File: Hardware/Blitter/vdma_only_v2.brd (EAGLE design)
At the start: 100 x 157.5 mm, 82 parts, among them IC1 74S08N, IC10 74HC191N, IC11 74HC191N, IC12 74HC191N, IC13 74HC191N, IC14 74HC191N, IC15 74HC191N, IC16 74HC573N, IC17 74HC573N, IC18 7432N, IC19 74LS257N, IC2 74HC191N, IC20 7430N, IC21 7400N, IC22 74LS257N, IC23 74LS257N, IC24 74LS257N, IC25 74LS257N, IC26 74LS257N, IC27 74LS257N, IC28 74LS257N, IC29 74LS257N, IC3 74HC573N, IC30 74HC573N, IC31 7400N, IC32 7432N, IC4 74HC191N, IC5 74HC573N, IC53 7404N, IC54 74LS07N, IC6 74HC573N, IC7 74HC573N, IC8 74HC573N, IC9 74LS74N, J1 TX25-40P-6ST-H1E, J2 TX25-40P-6ST-H1E

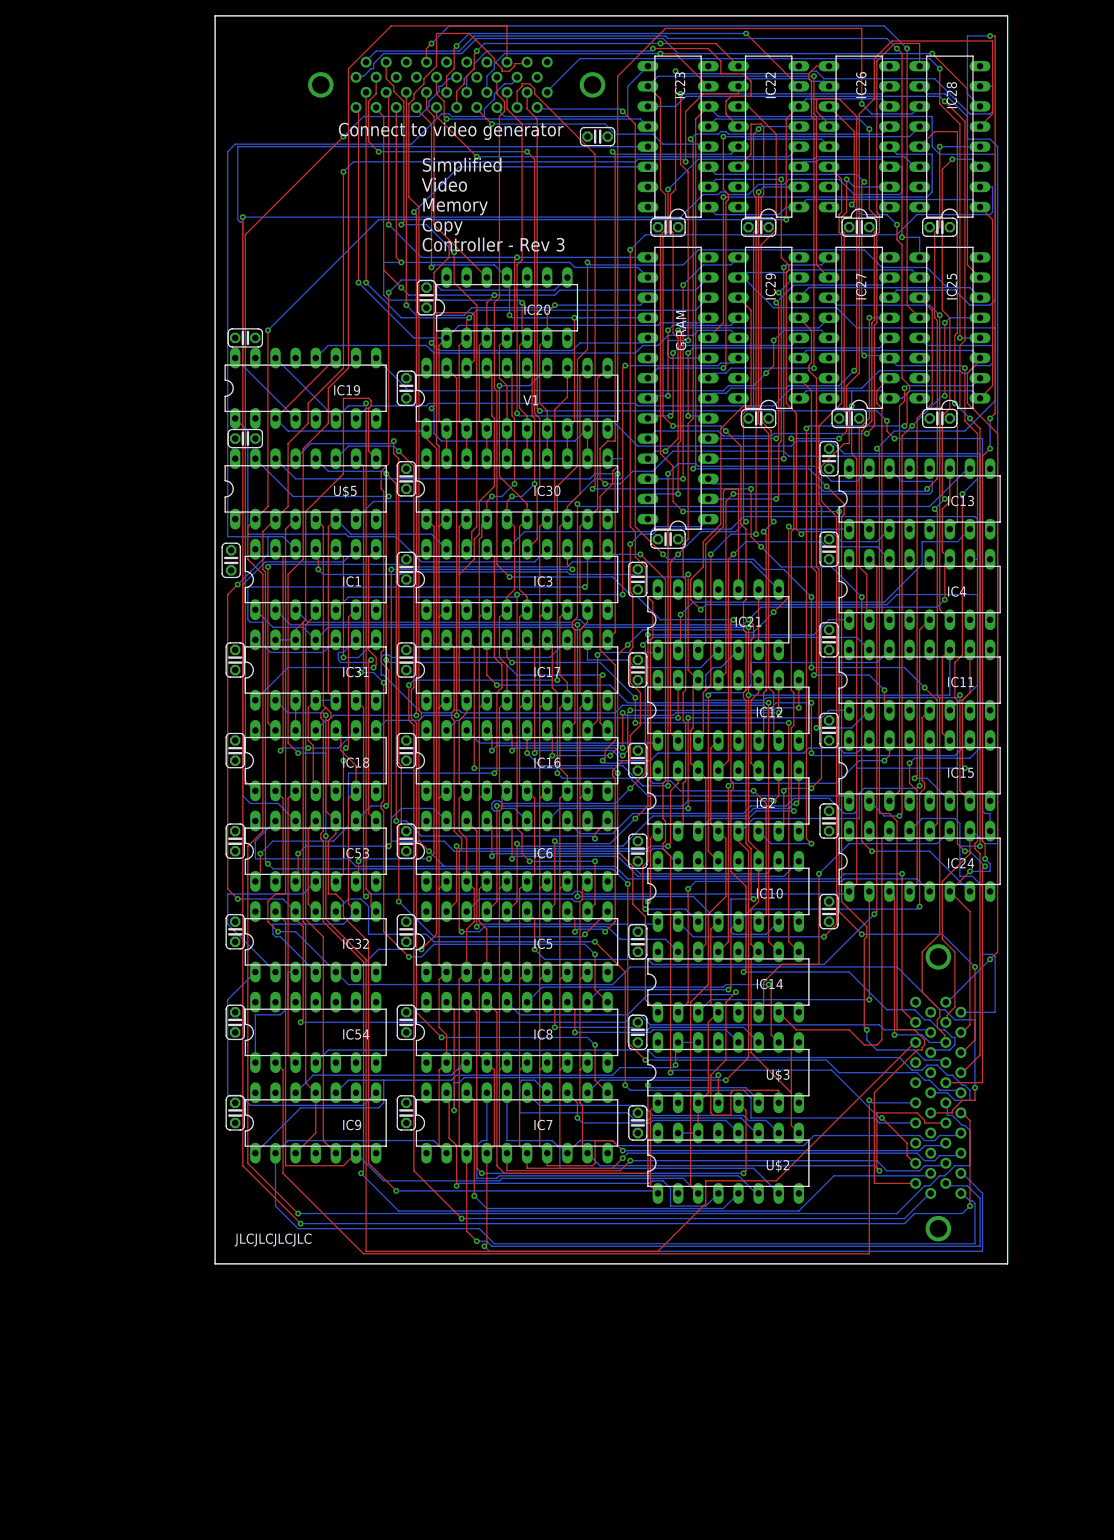
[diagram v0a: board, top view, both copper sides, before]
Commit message: update blitter
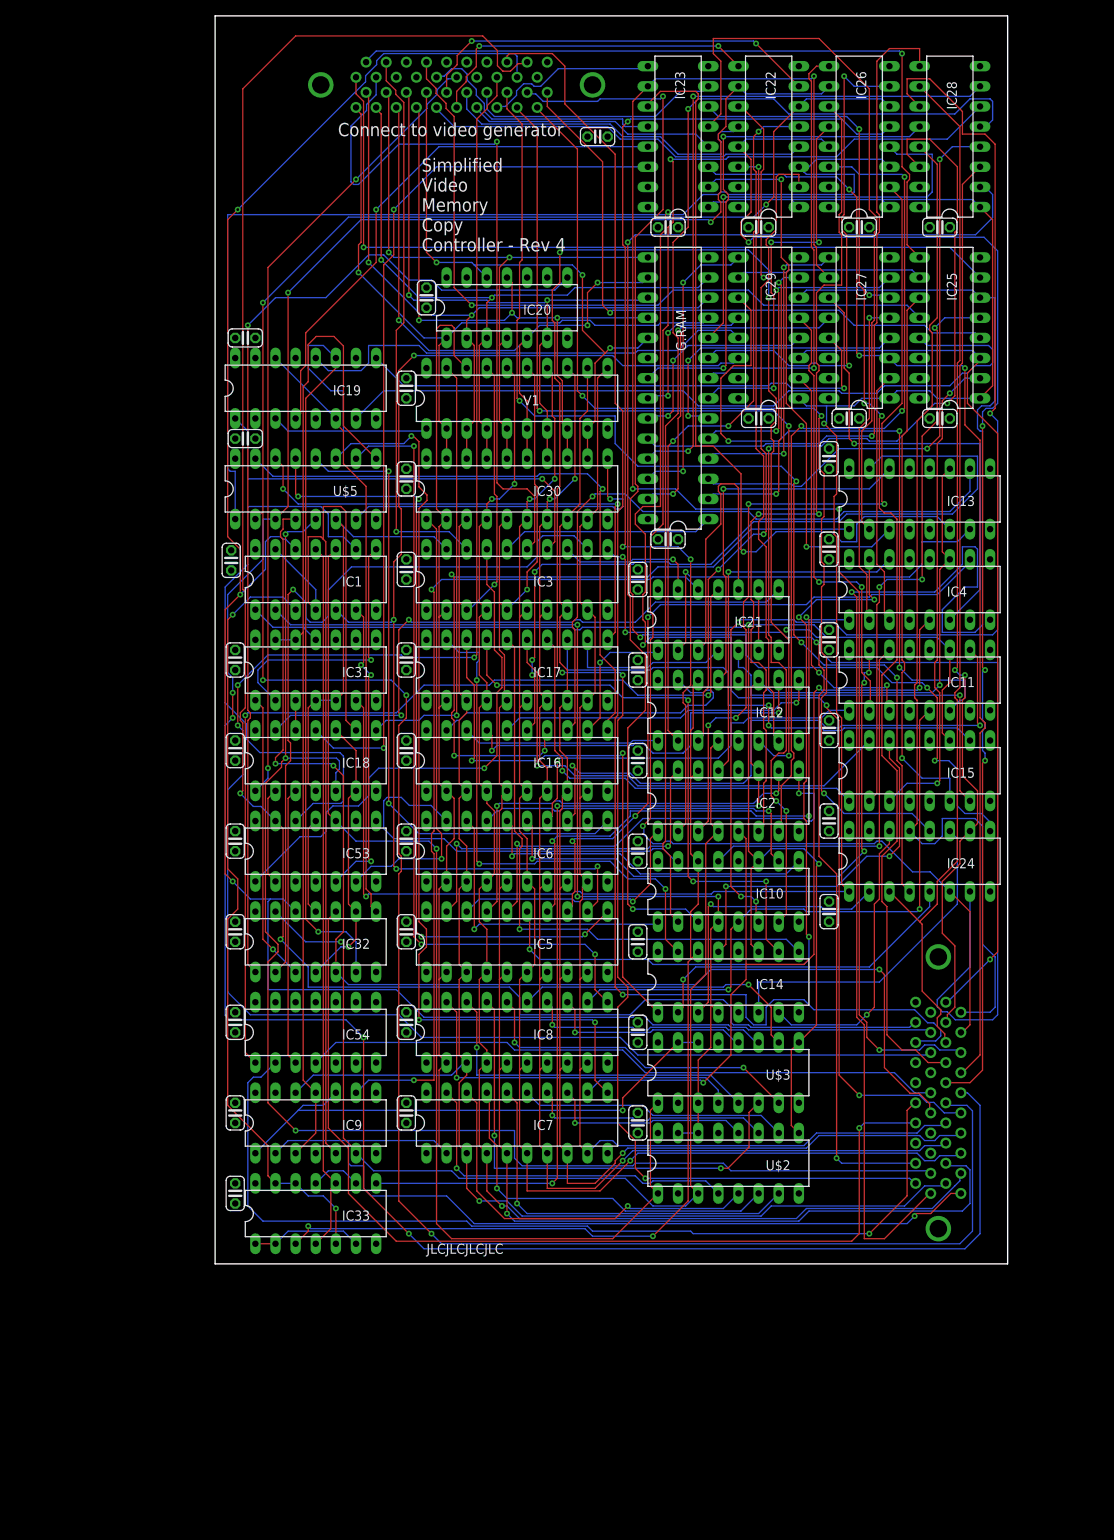
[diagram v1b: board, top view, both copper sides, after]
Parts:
- added C41: (no value), rcl:C025-024X044
- added IC33: 7400N, 74xx-us:DIL14
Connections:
- removed net !DMAIRQEN: IC32.2, IC53.4
- removed net N$100: IC32.1, IC9.8
- removed net N$213: IC20.8, IC53.9
- removed net N$214: IC31.9, IC53.8
- new net N$47: IC1.3, IC33.12, IC33.13, IC33.5
- new net N$48: IC33.11, IC33.9
- new net N$49: IC33.1, IC33.2, IC33.6
- new net N$58: IC21.12, IC9.9
- new net N$66: IC20.8, IC32.1
- new net XCLK: IC10.14, IC12.14, IC14.14, IC2.14, IC33.3
- net !DMACLK!/!IDLE!: now also IC1.10; no longer IC31.2
- net !DMAIRQ: now also IC21.11; no longer IC32.3
- net !XRELOAD: now also IC33.8; no longer IC1.3
- net DMACLK/!IDLE!: now also IC33.10, IC33.4; no longer IC10.14, IC12.14, IC14.14, IC2.14
- net DMAIRQEN: now also IC21.13; no longer IC53.3
- net GND: now also C41.2, IC31.10, IC31.9, IC33.7, IC53.3, IC53.9
- net N$16: now also IC31.1, IC32.3; no longer IC1.10, IC31.8
- net N$39: now also IC31.2; no longer IC31.1
- net TRANSEN: now also IC32.2; no longer IC31.10
- net VCC: now also C41.1, IC33.14
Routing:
- net N$66: track 0.00 -> 128.8 mm, vias 0 -> 1
- net XCLK: track 0.00 -> 122.9 mm, vias 0 -> 2
- net N$58: track 0.00 -> 107.8 mm, vias 0 -> 2
- net !DMAIRQ: track 16.0 -> 119.3 mm, vias 0 -> 2
- net N$47: track 0.00 -> 98.5 mm, vias 0 -> 2
- net N$213: track 94.9 -> 0.00 mm, vias 2 -> 0
- net CLK7: track 267.2 -> 181.7 mm, vias 2 -> 1
- net A12: track 276.1 -> 200.2 mm, vias 4 -> 1
- net A5: track 222.0 -> 152.7 mm, vias 3 -> 4
- net CLK3_5: track 175.5 -> 237.9 mm
- net DMAIRQEN: track 76.2 -> 18.2 mm, vias 4 -> 1
- net A2: track 274.0 -> 323.2 mm, vias 5 -> 6
- net N$37: track 111.5 -> 62.7 mm
- net VA8: track 149.1 -> 196.3 mm, vias 5 -> 3
- net A8: track 145.1 -> 190.6 mm, vias 5 -> 2
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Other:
- board text added: "Designed by Clyde Shaffer December 2020"
- board text added: "Simplified Video Memory Copy Controller - Rev 4"
- board text removed: "Designed by Clyde Shaffer November 2020"
- board text removed: "Simplified Video Memory Copy Controller - Rev 3"

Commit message: regrettably I don't remember what I changed since the last commit
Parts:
- removed IC10, IC11, IC12, IC13, IC14, IC15, IC2, IC4: 74HC191N, 74xx-us:DIL16
- removed IC16, IC17, IC3, IC30, IC5, IC6, IC7, IC8: 74HC573N, 74xx-us:DIL20
- removed IC19, IC22, IC23, IC24, IC25, IC26, IC27, IC28, IC29: 74LS257N, 74xx-us:DIL16
- removed IC33: 7400N, 74xx-us:DIL14
- removed U$2, U$3: CD40103, 000_mychips2:DIL16
- added BANKMUX, GMUX0, GMUX1, GMUX2, GMUX3, VMUX0, VMUX1, VMUX2, VMUX3: 74LS257N, 74xx-us:DIL16
- added CTR.H, CTR.W: CD40103, 000_mychips2:DIL16
- added GXFLIPPER, GYFLIPPER: 74AHC8541, 0_gametankparts:DIL20
- added GXH, GXL, GYH, GYL, VXH, VXL, VYH, VYL: 74HC163, 0_gametankparts:DIL16
- added PAD1, PAD2: (no value), wirepad:2,54/0,9
- added REG.COLOR, REG.FLAGS, REG.GX, REG.GY, REG.H, REG.VX, REG.VY, REG.W: 74HC573N, 74xx-us:DIL20
- moved C5 114.9 mm to (63.5, 2.54), turned to 0 degrees
- moved C27 80.3 mm to (52.1, 2.54), turned to 0 degrees
- moved C8 79.6 mm to (90.2, 109.2), turned to 0 degrees
- moved C31 76.0 mm to (78.7, 55.9)
- moved C32 76.0 mm to (68.6, 55.9)
- moved C33 76.0 mm to (55.9, 55.9)
- moved C34 76.0 mm to (44.5, 55.9)
- moved C29 75.5 mm to (55.9, 128.3), turned to 0 degrees
- moved C28 74.5 mm to (40.6, 2.54), turned to 0 degrees
- moved C25 74.3 mm to (52.1, 31.8), turned to 0 degrees
- moved C9 71.8 mm to (74.9, 2.54), turned to 0 degrees
- moved C26 69.1 mm to (40.6, 31.8), turned to 0 degrees
- moved C21 63.8 mm to (78.7, 109.2), turned to 0 degrees
- moved C24 63.7 mm to (78.7, 133.3), turned to 0 degrees
- moved C36 59.7 mm to (90.2, 133.3), turned to 0 degrees
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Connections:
- removed net N$107: IC12.13, IC13.14
- removed net N$109: IC14.13, IC15.14
- removed net XCLK: IC10.14, IC12.14, IC14.14, IC2.14, IC33.3
- new net GX-CARRY: GXH.10, GXL.15
- new net GY-CARRY: GYH.10, GYL.15
- new net N$68: GXFLIPPER.7, GXH.13
- new net N$72: GXFLIPPER.8, GXH.12
- new net N$73: GYFLIPPER.2, GYL.14
- new net N$74: GYFLIPPER.3, GYL.13
- new net N$75: GYFLIPPER.4, GYL.12
- new net N$76: GYFLIPPER.5, GYL.11
- new net N$77: GYFLIPPER.6, GYH.14
- new net N$78: GYFLIPPER.7, GYH.13
- new net N$79: GYFLIPPER.8, GYH.12
- new net N$80: GYFLIPPER.1, IC53.4
- new net N$81: GXFLIPPER.1, IC31.8
- new net ROWCOMPLETE: GYL.10, IC53.8, VYL.10
- new net VX-CARRY: VXH.10, VXL.15
- new net VY-CARRY: VYH.10, VYL.15
- net !COPYDONE: now also CTR.H.14, CTR.H.15; no longer U$3.14, U$3.15
- net !DMA-ENABLED: now also CTR.W.3; no longer IC12.4, IC2.4, U$2.3
- net !DMACLK!/!IDLE!: now also CTR.H.1, CTR.W.1; no longer U$2.1, U$3.1
- net !DMAMODE: now also GMUX0.1, GMUX1.1, GMUX2.1, GMUX3.1, VMUX0.1, VMUX1.1, VMUX2.1, VMUX3.1; no longer IC22.1, IC23.1, IC24.1, IC25.1, IC26.1, IC27.1, IC28.1, IC29.1
- net !DMASTART: now also CTR.H.9, CTR.W.9, GYH.9, GYL.9, VYH.9, VYL.9; no longer IC10.11, IC11.11, IC14.11, IC15.11, U$2.9, U$3.9
- net !ROWCOMPLETE: now also CTR.H.3, CTR.W.14, CTR.W.15, IC53.9; no longer IC10.4, IC14.4, U$2.14, U$2.15, U$3.3
- net !VOE: now also VMUX3.12; no longer IC25.12
- net !VWE: now also VMUX1.12; no longer IC23.12
- net !WRAP_X: now also REG.VX.12; no longer IC16.12
- net !WRAP_Y: now also REG.VY.12; no longer IC17.12
- net !XRELOAD: now also GXH.9, GXL.9, IC1.3, VXH.9, VXL.9; no longer IC12.11, IC13.11, IC2.11, IC33.8, IC4.11
- net A0: now also GMUX0.3, VMUX0.3; no longer IC22.3, IC26.3
- net A1: now also GMUX0.6, VMUX0.6; no longer IC22.6, IC26.6
- net A10: now also GMUX2.13, VMUX2.13; no longer IC24.13, IC28.13
- net A11: now also GMUX3.3, VMUX3.3; no longer IC25.3, IC29.3
- net A12: now also GMUX3.6, VMUX3.6; no longer IC25.6, IC29.6
- net A13: now also GMUX3.10, VMUX3.10; no longer IC25.10, IC29.10
- net A2: now also GMUX0.10, VMUX0.10; no longer IC22.10, IC26.10
- net A3: now also GMUX0.13, VMUX0.13; no longer IC22.13, IC26.13
- net A4: now also GMUX1.3, VMUX1.3; no longer IC23.3, IC27.3
- net A5: now also GMUX1.6, VMUX1.6; no longer IC23.6, IC27.6
- net A6: now also GMUX1.10, VMUX1.10; no longer IC23.10, IC27.10
- net A7: now also GMUX2.3, VMUX2.3; no longer IC24.3, IC28.3
- net A8: now also GMUX2.6, VMUX2.6; no longer IC24.6, IC28.6
- net A9: now also GMUX2.10, VMUX2.10; no longer IC24.10, IC28.10
- net COLORFILL: now also GMUX3.14, REG.GX.12; no longer IC29.14, IC5.12
- net D0: now also REG.COLOR.2, REG.FLAGS.2, REG.GX.2, REG.GY.2, REG.H.2, REG.VX.2, REG.VY.2, REG.W.2; no longer IC16.2, IC17.2, IC3.2, IC30.2, IC5.2, IC6.2, IC7.2, IC8.2
- net D1: now also REG.COLOR.3, REG.FLAGS.3, REG.GX.3, REG.GY.3, REG.H.3, REG.VX.3, REG.VY.3, REG.W.3; no longer IC16.3, IC17.3, IC3.3, IC30.3, IC5.3, IC6.3, IC7.3, IC8.3
- net D2: now also REG.COLOR.4, REG.FLAGS.4, REG.GX.4, REG.GY.4, REG.H.4, REG.VX.4, REG.VY.4, REG.W.4; no longer IC16.4, IC17.4, IC3.4, IC30.4, IC5.4, IC6.4, IC7.4, IC8.4
- net D3: now also REG.COLOR.5, REG.FLAGS.5, REG.GX.5, REG.GY.5, REG.H.5, REG.VX.5, REG.VY.5, REG.W.5; no longer IC16.5, IC17.5, IC3.5, IC30.5, IC5.5, IC6.5, IC7.5, IC8.5
- net D4: now also REG.COLOR.6, REG.FLAGS.6, REG.GX.6, REG.GY.6, REG.H.6, REG.VX.6, REG.VY.6, REG.W.6; no longer IC16.6, IC17.6, IC3.6, IC30.6, IC5.6, IC6.6, IC7.6, IC8.6
- net D5: now also REG.COLOR.7, REG.FLAGS.7, REG.GX.7, REG.GY.7, REG.H.7, REG.VX.7, REG.VY.7, REG.W.7; no longer IC16.7, IC17.7, IC3.7, IC30.7, IC5.7, IC6.7, IC7.7, IC8.7
- net D6: now also REG.COLOR.8, REG.FLAGS.8, REG.GX.8, REG.GY.8, REG.H.8, REG.VX.8, REG.VY.8, REG.W.8; no longer IC16.8, IC17.8, IC3.8, IC30.8, IC5.8, IC6.8, IC7.8, IC8.8
- net D7: now also REG.COLOR.9, REG.FLAGS.9, REG.GX.9, REG.GY.9, REG.H.9, REG.VX.9, REG.VY.9, REG.W.9; no longer IC16.9, IC17.9, IC3.9, IC30.9, IC5.9, IC6.9, IC7.9, IC8.9
- net DD0: now also REG.COLOR.19; no longer IC30.19
- net DD1: now also REG.COLOR.18; no longer IC30.18
- net DD2: now also REG.COLOR.17; no longer IC30.17
- net DD3: now also REG.COLOR.16; no longer IC30.16
- net DD4: now also REG.COLOR.15; no longer IC30.15
- net DD5: now also REG.COLOR.14; no longer IC30.14
- net DD6: now also REG.COLOR.13; no longer IC30.13
- net DD7: now also REG.COLOR.12; no longer IC30.12
- net DMA-ENABLED: now also GXH.7, GXL.7, GYH.7, GYL.7, VXH.7, VXL.7, VYH.7, VYL.7; no longer IC1.13
- net DMACLK/!IDLE!: now also GXH.2, GXL.2, GYH.2, GYL.2, VXH.2, VXL.2, VYH.2, VYL.2; no longer IC33.10, IC33.4
- net DMAIRQEN: now also REG.FLAGS.13; no longer IC3.13
- net DMAMODE: now also REG.FLAGS.19; no longer IC3.19
- net GND: now also BANKMUX.15, BANKMUX.8, CTR.H.13, CTR.H.8, CTR.W.13, CTR.W.8, GMUX0.15, GMUX0.8, GMUX1.15, GMUX1.8, GMUX2.15, GMUX2.8, GMUX3.15, GMUX3.8, GXFLIPPER.10, GXFLIPPER.11, GXH.8, GXL.8, GYFLIPPER.10, GYFLIPPER.11, GYH.8, GYL.8, PAD1.1, PAD2.1, REG.COLOR.10, REG.FLAGS.1, REG.FLAGS.10, REG.GX.1, REG.GX.10, REG.GY.1, REG.GY.10, REG.H.1, REG.H.10, REG.VX.1, REG.VX.10, REG.VY.1, REG.VY.10, REG.W.1, REG.W.10, VMUX0.15, VMUX0.8, VMUX1.15, VMUX1.8, VMUX2.15, VMUX2.8, VMUX3.15, VMUX3.8, VXH.8, VXL.8, VYH.8, VYL.8; no longer IC10.8, IC11.4, IC11.8, IC11.9, IC12.5, IC12.8, IC13.4, IC13.5, IC13.8, IC13.9, IC14.5, IC14.8, IC15.4, IC15.5, IC15.8, IC15.9, IC16.1, IC16.10, IC17.1, IC17.10, IC19.15, IC19.8, IC2.8, IC22.15, IC22.8, IC23.15, IC23.8, IC24.15, IC24.8, IC25.15, IC25.8, IC26.15, IC26.8, IC27.15, IC27.8, IC28.15, IC28.8, IC29.15, IC29.8, IC3.1, IC3.10, IC30.10, IC31.10, IC31.9, IC33.7, IC4.4, IC4.8, IC4.9, IC5.1, IC5.10, IC53.3, IC53.9, IC6.1, IC6.10, IC7.1, IC7.10, IC8.1, IC8.10, U$2.13, U$2.8, U$3.13, U$3.8
- net GRAMBANK: now also REG.FLAGS.16; no longer IC3.16
- net N$1: now also GMUX0.4; no longer IC26.4
- net N$10: now also GMUX2.9; no longer IC28.9
- net N$108: now also REG.W.11; no longer IC7.11
- net N$11: now also GMUX2.12; no longer IC28.12
- net N$111: now also REG.H.11; no longer IC8.11
- net N$113: now also REG.VY.19, VYL.3; no longer IC14.15, IC17.19
- net N$114: now also REG.VY.18, VYL.4; no longer IC14.1, IC17.18
- net N$115: now also REG.VY.17, VYL.5; no longer IC14.10, IC17.17
- net N$116: now also REG.VY.16, VYL.6; no longer IC14.9, IC17.16
- net N$117: now also REG.VX.15, VXH.3; no longer IC13.15, IC16.15
- net N$118: now also REG.VX.14, VXH.4; no longer IC13.1, IC16.14
- net N$119: now also REG.VX.13, VXH.5; no longer IC13.10, IC16.13
- net N$12: now also GMUX3.4; no longer IC29.4
- net N$121: now also REG.VX.19, VXL.3; no longer IC12.15, IC16.19
- net N$122: now also REG.VX.18, VXL.4; no longer IC12.1, IC16.18
- net N$123: now also REG.VX.17, VXL.5; no longer IC12.10, IC16.17
- net N$124: now also REG.VX.16, VXL.6; no longer IC12.9, IC16.16
- net N$125: now also REG.COLOR.11; no longer IC30.11
- net N$13: now also GMUX3.7; no longer IC29.7
- net N$14: now also GMUX3.9; no longer IC29.9
- net N$15: now also VMUX1.14; no longer IC23.14
- net N$160: now also VMUX0.5, VXL.13; no longer IC12.2, IC22.5
- net N$161: now also VMUX0.11, VXL.12; no longer IC12.6, IC22.11
- net N$162: now also VMUX0.14, VXL.11; no longer IC12.7, IC22.14
- net N$163: now also VMUX1.2, VXH.14; no longer IC13.3, IC23.2
- net N$164: now also VMUX1.5, VXH.13; no longer IC13.2, IC23.5
- net N$165: now also VMUX1.11, VXH.12; no longer IC13.6, IC23.11
- net N$167: now also VMUX2.5, VYL.13; no longer IC14.2, IC24.5
- net N$168: now also VMUX2.11, VYL.12; no longer IC14.6, IC24.11
- net N$169: now also VMUX2.14, VYL.11; no longer IC14.7, IC24.14
- net N$17: now also GMUX1.12; no longer IC27.12
- net N$170: now also VMUX3.2, VYH.14; no longer IC15.3, IC25.2
- net N$171: now also VMUX3.5, VYH.13; no longer IC15.2, IC25.5
- net N$172: now also VMUX3.11, VYH.12; no longer IC15.6, IC25.11
- net N$173: now also GMUX0.2, GXFLIPPER.19; no longer IC2.3, IC26.2
- net N$174: now also GMUX0.5, GXFLIPPER.18; no longer IC2.2, IC26.5
- net N$175: now also GMUX0.11, GXFLIPPER.17; no longer IC2.6, IC26.11
- net N$176: now also GMUX0.14, GXFLIPPER.16; no longer IC2.7, IC26.14
- net N$177: now also GMUX1.2, GXFLIPPER.15; no longer IC27.2, IC4.3
- net N$178: now also GMUX1.5, GXFLIPPER.14; no longer IC27.5, IC4.2
- net N$179: now also GMUX1.11, GXFLIPPER.13; no longer IC27.11, IC4.6
- net N$18: now also GMUX3.12; no longer IC29.12
- net N$180: now also GMUX2.2, GYFLIPPER.19; no longer IC10.3, IC28.2
- net N$181: now also GMUX2.5, GYFLIPPER.18; no longer IC10.2, IC28.5
- net N$182: now also GMUX2.11, GYFLIPPER.17; no longer IC10.6, IC28.11
- net N$183: now also GMUX2.14, GYFLIPPER.16; no longer IC10.7, IC28.14
- net N$184: now also GMUX3.2, GYFLIPPER.15; no longer IC11.3, IC29.2
- net N$185: now also GMUX3.5, GYFLIPPER.14; no longer IC11.2, IC29.5
- net N$186: now also GMUX3.11, GYFLIPPER.13; no longer IC11.6, IC29.11
- net N$19: now also GYL.3, REG.GY.19; no longer IC10.15, IC6.19
- net N$2: now also GMUX0.7; no longer IC26.7
- net N$20: now also GYL.4, REG.GY.18; no longer IC10.1, IC6.18
- net N$21: now also GYL.5, REG.GY.17; no longer IC10.10, IC6.17
- net N$22: now also GYL.6, REG.GY.16; no longer IC10.9, IC6.16
- net N$23: now also GXH.3, REG.GX.15; no longer IC4.15, IC5.15
- net N$24: now also GXH.4, REG.GX.14; no longer IC4.1, IC5.14
- net N$25: now also GXH.5, REG.GX.13; no longer IC4.10, IC5.13
- net N$26: now also GYH.3, REG.GY.15; no longer IC11.15, IC6.15
- net N$27: now also GXL.3, REG.GX.19; no longer IC2.15, IC5.19
- net N$28: now also GXL.4, REG.GX.18; no longer IC2.1, IC5.18
- net N$29: now also GXL.5, REG.GX.17; no longer IC2.10, IC5.17
- net N$3: now also GMUX0.9; no longer IC26.9
- net N$30: now also GXL.6, REG.GX.16; no longer IC2.9, IC5.16
- net N$31: now also GYH.4, REG.GY.14; no longer IC11.1, IC6.14
- net N$32: now also GYH.5, REG.GY.13; no longer IC11.10, IC6.13
- net N$35: now also REG.VY.15, VYH.3; no longer IC15.15, IC17.15
- net N$36: now also REG.VY.14, VYH.4; no longer IC15.1, IC17.14
- net N$37: now also REG.VY.13, VYH.5; no longer IC15.10, IC17.13
- net N$4: now also GMUX0.12; no longer IC26.12
- net N$41: now also REG.COLOR.1; no longer IC30.1
- net N$42: now also GXFLIPPER.5, GXL.11; no longer IC2.13, IC4.14
- net N$43: now also GXFLIPPER.4, GXL.12; no longer IC10.13, IC11.14
- net N$47: now also GXFLIPPER.3, GXL.13; no longer IC1.3, IC33.12, IC33.13, IC33.5
- net N$48: now also GXFLIPPER.2, GXL.14; no longer IC33.11, IC33.9
- net N$49: now also GXFLIPPER.6, GXH.14; no longer IC33.1, IC33.2, IC33.6
- net N$5: now also GMUX1.4; no longer IC27.4
- net N$50: now also BANKMUX.4, VMUX1.13; no longer IC19.4, IC23.13
- net N$51: now also CTR.H.4, REG.H.19; no longer IC8.19, U$3.4
- net N$52: now also CTR.H.5, REG.H.18; no longer IC8.18, U$3.5
- net N$53: now also CTR.H.6, REG.H.17; no longer IC8.17, U$3.6
- net N$54: now also CTR.H.7, REG.H.16; no longer IC8.16, U$3.7
- net N$55: now also CTR.H.10, REG.H.15; no longer IC8.15, U$3.10
- net N$56: now also CTR.H.11, REG.H.14; no longer IC8.14, U$3.11
- net N$57: now also CTR.H.12, REG.H.13; no longer IC8.13, U$3.12
- net N$59: now also CTR.W.4, REG.W.19; no longer IC7.19, U$2.4
- net N$6: now also GMUX1.7; no longer IC27.7
- net N$60: now also CTR.W.5, REG.W.18; no longer IC7.18, U$2.5
- net N$61: now also CTR.W.6, REG.W.17; no longer IC7.17, U$2.6
- net N$62: now also CTR.W.7, REG.W.16; no longer IC7.16, U$2.7
- net N$63: now also CTR.W.10, REG.W.15; no longer IC7.15, U$2.10
- net N$64: now also CTR.W.11, REG.W.14; no longer IC7.14, U$2.11
- net N$65: now also CTR.W.12, REG.W.13; no longer IC7.13, U$2.12
- net N$67: now also BANKMUX.7, VMUX3.13; no longer IC19.7, IC25.13
- net N$69: now also BANKMUX.9, GMUX1.13; no longer IC19.9, IC27.13
- net N$7: now also GMUX1.9; no longer IC27.9
- net N$70: now also BANKMUX.12, GMUX3.13; no longer IC19.12, IC29.13
- net N$71: now also REG.VX.11; no longer IC16.11
- net N$8: now also GMUX2.4; no longer IC28.4
- net N$9: now also GMUX2.7; no longer IC28.7
- net N$94: now also REG.VY.11; no longer IC17.11
- net N$96: now also REG.GX.11; no longer IC5.11
- net N$98: now also REG.GY.11; no longer IC6.11
- net OFFSCR_X: now also VXH.11; no longer IC13.7
- net OFFSCR_Y: now also VYH.11; no longer IC15.7
- net TRANSEN: now also REG.FLAGS.12; no longer IC3.12
- net V/_G: now also BANKMUX.1, REG.FLAGS.14; no longer IC19.1, IC3.14
- net VA0: now also VMUX0.4; no longer IC22.4
- net VA1: now also VMUX0.7; no longer IC22.7
- net VA10: now also VMUX2.12; no longer IC24.12
- net VA11: now also VMUX3.4; no longer IC25.4
- net VA12: now also VMUX3.7; no longer IC25.7
- net VA13: now also VMUX3.9; no longer IC25.9
- net VA2: now also VMUX0.9; no longer IC22.9
- net VA3: now also VMUX0.12; no longer IC22.12
- net VA4: now also VMUX1.4; no longer IC23.4
- net VA5: now also VMUX1.7; no longer IC23.7
- net VA6: now also VMUX1.9; no longer IC23.9
- net VA7: now also VMUX2.4; no longer IC24.4
- net VA8: now also VMUX2.7; no longer IC24.7
- net VA9: now also VMUX2.9; no longer IC24.9
- net VCC: now also BANKMUX.10, BANKMUX.13, BANKMUX.16, BANKMUX.2, BANKMUX.5, CTR.H.16, CTR.H.2, CTR.W.16, CTR.W.2, GMUX0.16, GMUX1.14, GMUX1.16, GMUX2.16, GMUX3.16, GXFLIPPER.20, GXH.1, GXH.16, GXL.1, GXL.10, GXL.16, GYFLIPPER.20, GYH.1, GYH.16, GYL.1, GYL.16, IC1.13, REG.COLOR.20, REG.FLAGS.20, REG.GX.20, REG.GY.20, REG.H.20, REG.VX.20, REG.VY.20, REG.W.20, VMUX0.16, VMUX1.16, VMUX2.16, VMUX3.14, VMUX3.16, VXH.1, VXH.16, VXL.1, VXL.10, VXL.16, VYH.1, VYH.16, VYL.1, VYL.16; no longer IC10.16, IC11.16, IC12.16, IC13.16, IC14.16, IC15.16, IC16.20, IC17.20, IC19.10, IC19.13, IC19.16, IC19.2, IC19.5, IC2.16, IC22.16, IC23.16, IC24.16, IC25.14, IC25.16, IC26.16, IC27.14, IC27.16, IC28.16, IC29.16, IC3.20, IC30.20, IC33.14, IC4.16, IC5.20, IC6.20, IC7.20, IC8.20, U$2.16, U$2.2, U$3.16, U$3.2
- net VG_OE: now also BANKMUX.14, BANKMUX.6; no longer IC19.14, IC19.6
- net VG_WE: now also BANKMUX.11, BANKMUX.3; no longer IC19.11, IC19.3
- net VIDFLAGS: now also REG.FLAGS.11; no longer IC3.11
- net VIDPAGE: now also REG.FLAGS.18; no longer IC3.18
- net VNMI_ENABLE: now also REG.FLAGS.17; no longer IC3.17
- net VRAMBANK: now also REG.FLAGS.15; no longer IC3.15
- net XDIR: now also IC31.10, IC31.9, REG.W.12; no longer IC2.5, IC4.5, IC7.12
- net XODD: now also VMUX0.2, VXL.14; no longer IC12.3, IC22.2
- net YDIR: now also IC53.3, REG.H.12; no longer IC10.5, IC11.5, IC8.12
- net YODD: now also VMUX2.2, VYL.14; no longer IC14.3, IC24.2
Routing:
- net A2: track 323.2 -> 0.00 mm, vias 6 -> 0
- net A0: track 295.7 -> 0.00 mm, vias 4 -> 0
- net CLK14: track 254.0 -> 0.00 mm, vias 3 -> 0
- net CLK28: track 243.6 -> 0.00 mm, vias 2 -> 0
- net CLK3_5: track 237.9 -> 0.00 mm, vias 3 -> 0
- net D0: track 229.6 -> 0.00 mm, vias 1 -> 0
- net !DMAMODE: track 237.6 -> 14.6 mm, vias 2 -> 0
- net A1: track 321.5 -> 104.4 mm, vias 5 -> 0
- net A13: track 214.2 -> 0.00 mm, vias 4 -> 0
- net D1: track 210.1 -> 0.00 mm, vias 2 -> 0
- net A6: track 207.7 -> 0.00 mm, vias 4 -> 0
- net A12: track 200.2 -> 0.00 mm, vias 1 -> 0
- net VA8: track 196.3 -> 0.00 mm, vias 3 -> 0
- net D3: track 195.3 -> 0.00 mm, vias 2 -> 0
- net !DMASTART: track 192.2 -> 0.00 mm, vias 2 -> 0
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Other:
- board text added: "Designed by Clyde Shaffer January 2021"
- board text added: "Simplified Video Memory Copy Controller - Rev 5"
- board text removed: "Designed by Clyde Shaffer December 2020"
- board text removed: "Simplified Video Memory Copy Controller - Rev 4"

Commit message: Blitter V6 w/ 4-phase clock
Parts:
- added C42, C43, C44, C46: (no value), rcl:C025-024X044
- added CLK.SEQ: 74ALS08N, 74xx-us:DIL14
- added IC2: 74ALS04N, 74xx-us:DIL14
- added IC5: 74ALS00N, 74xx-us:DIL14
- added TRIGGER.INIT: 74LS74N, 74xx-us:DIL14
- moved BANKMUX 11.4 mm to (81.3, 67.3)
- moved C21 11.4 mm to (90.2, 109.2)
- moved C22 11.4 mm to (74.9, 31.8)
- moved C24 11.4 mm to (90.2, 133.3)
- moved C31 11.4 mm to (90.2, 55.9)
- moved C32 11.4 mm to (80.0, 55.9)
- moved C40 11.4 mm to (90.2, 80.0)
- moved C5 11.4 mm to (74.9, 2.54)
- moved G.RAM 11.4 mm to (81.3, 137.2)
- moved GMUX0 11.4 mm to (104.1, 120.7)
- moved GMUX1 11.4 mm to (104.1, 144.8)
- moved GXFLIPPER 11.4 mm to (104.1, 94.0)
- moved GXH 11.4 mm to (104.1, 67.3)
- moved GXL 11.4 mm to (88.9, 43.2)
- moved J1 11.4 mm to (106.7, 21.6)
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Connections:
- net !DMAIRQ renamed !IRQ-OUT
- net DMAIRQEN renamed IRQ-ENABLE
- net N$58 renamed IRQ
- removed net !CLK28: IC1.9, IC53.12
- removed net !DMA-ENABLED: CTR.W.3, IC32.13, IC9.6
- removed net !DMACLK!/!IDLE!: CTR.H.1, CTR.W.1, IC1.10, IC53.10
- removed net !DMASTART: CTR.H.9, CTR.W.9, GYH.9, GYL.9, IC1.1, IC31.11, VYH.9, VYL.9
- removed net DMA-ENABLED: GXH.7, GXL.7, GYH.7, GYL.7, IC1.4, IC18.9, IC9.5, VXH.7, VXL.7, VYH.7, VYL.7
- removed net DMACLK/!IDLE!: GXH.2, GXL.2, GYH.2, GYL.2, IC1.11, VXH.2, VXL.2, VYH.2, VYL.2
- removed net DMACLK/IDLE: IC32.11, IC53.11
- removed net DMASTART: IC31.12, IC31.13, IC9.11, IC9.3, U$5.9
- new net !INIT: CTR.H.15, CTR.W.15, GYH.9, GYL.9, IC1.1, TRIGGER.INIT.1, TRIGGER.INIT.8, VYH.9, VYL.9
- new net !RUNNING: CTR.W.3, IC9.6
- new net !TRIGGER: IC31.11, TRIGGER.INIT.4
- new net N$58: IC31.10, TRIGGER.INIT.9
- new net N$82: IC31.8, IC9.4, TRIGGER.INIT.13
- new net N$83: CLK.SEQ.13, IC2.6
- new net N$84: CLK.SEQ.12, IC2.8
- new net N$85: CLK.SEQ.5, IC2.2
- new net N$86: CLK.SEQ.9, IC2.4
- new net N$87: CTR.W.9, IC5.3
- new net N$88: IC2.10, IC9.13
- new net P0: CLK.SEQ.11, CTR.W.1
- new net P1: CLK.SEQ.8, CTR.H.1, GXH.2, GXL.2, GYH.2, GYL.2, VXH.2, VXL.2, VYH.2, VYL.2
- new net P2: CLK.SEQ.6, IC31.9, IC5.1
- new net P3: CLK.SEQ.3, IC1.10, TRIGGER.INIT.11
- new net RUNNING: GXH.7, GXL.7, GYH.7, GYL.7, IC1.4, IC1.9, IC18.9, IC9.5, VXH.7, VXL.7, VYH.7, VYL.7
- new net TRIGGER-FLAG: TRIGGER.INIT.12, TRIGGER.INIT.5
- new net TRIGGER-SELECT: IC2.11, IC31.12, U$5.9
- net !COPYDONE: no longer CTR.H.15
- net !ROWCOMPLETE: no longer CTR.W.15
- net CLK14: now also CLK.SEQ.1, CLK.SEQ.4, IC2.3, IC2.9; no longer IC1.12, IC32.12
- net CLK28: now also CLK.SEQ.10, CLK.SEQ.2, IC2.1, IC2.5; no longer IC53.13
- net D0: now also IC31.13; no longer IC9.2
- net D1: no longer IC9.12
- net GND: now also C42.2, C43.2, C44.2, C46.2, CLK.SEQ.7, IC2.7, IC5.7, IC9.11, IC9.12, IC9.2, IC9.3, TRIGGER.INIT.2, TRIGGER.INIT.3, TRIGGER.INIT.7
- net N$81: now also IC53.12; no longer IC31.8
- net ROWCOMPLETE: now also IC5.2
- net VCC: now also C42.1, C43.1, C44.1, C46.1, CLK.SEQ.14, CTR.H.9, IC2.14, IC5.14, TRIGGER.INIT.10, TRIGGER.INIT.14; no longer IC1.13, IC9.13, IC9.4
- net XDIR: now also IC53.13; no longer IC31.10, IC31.9
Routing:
- net D1: track 0.00 -> 398.1 mm, vias 0 -> 3
- net D3: track 0.00 -> 368.5 mm, vias 0 -> 4
- net D0: track 0.00 -> 354.6 mm, vias 0 -> 3
- net COLORFILL: track 0.00 -> 347.8 mm, vias 0 -> 6
- net CLK3_5: track 0.00 -> 321.4 mm, vias 0 -> 3
- net D5: track 46.3 -> 352.6 mm, vias 0 -> 5
- net CLK28: track 0.00 -> 262.3 mm, vias 0 -> 2
- net D4: track 0.00 -> 253.1 mm, vias 0 -> 5
- net D6: track 0.00 -> 248.0 mm, vias 0 -> 3
- net A12: track 0.00 -> 247.2 mm, vias 0 -> 2
- net D2: track 0.00 -> 245.4 mm, vias 0 -> 3
- net A0: track 0.00 -> 239.6 mm, vias 0 -> 5
- net D7: track 16.2 -> 253.8 mm, vias 0 -> 5
- net CLK14: track 0.00 -> 228.6 mm, vias 0 -> 3
- net VIDPAGE: track 0.00 -> 223.1 mm, vias 0 -> 1
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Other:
- board size 100 x 157.5 mm -> 111.4 x 157.5 mm
- board text added: "Designed by Clyde Shaffer April 2021"
- board text added: "Simplified Video Memory Copy Controller - Rev 6"
- board text removed: "Designed by Clyde Shaffer January 2021"
- board text removed: "Simplified Video Memory Copy Controller - Rev 5"

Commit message: Blitter fixes
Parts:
- added IC3: 74LS86N, 74xx-us:DIL14
- added SJ1, SJ2, SJ3: (no value), jumper:SJ_2
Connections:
- removed net N$86: CLK.SEQ.9, IC2.4
- new net !SEQGEN_HIGH: CLK.SEQ.12, CLK.SEQ.5, IC3.8
- new net !SEQGEN_LOW: CLK.SEQ.10, CLK.SEQ.13, IC3.11
- new net N$89: IC3.1, IC3.13, SJ1.2
- new net P1LONG: CLK.SEQ.8, IC1.12
- new net SEQGEN_HIGH: CLK.SEQ.2, CLK.SEQ.9, IC3.6
- new net SEQGEN_LOW: CLK.SEQ.1, CLK.SEQ.4, IC3.3
- net CLK14: now also SJ2.3; no longer CLK.SEQ.1, CLK.SEQ.4, IC2.3, IC2.9
- net CLK28: now also IC53.11; no longer CLK.SEQ.10, CLK.SEQ.2, IC2.1, IC2.5
- net CLK3_5: now also SJ1.1
- net CLK7: now also SJ1.3, SJ2.1
- net GND: now also IC3.2, IC3.5, IC3.7
- net N$83: now also IC3.10, IC3.4, SJ2.2; no longer CLK.SEQ.13, IC2.6
- net N$84: now also IC53.10, SJ3.1; no longer CLK.SEQ.12, IC2.8
- net N$85: now also IC1.13, SJ3.2; no longer CLK.SEQ.5, IC2.2
- net P1: now also IC1.11; no longer CLK.SEQ.8
- net VCC: now also IC3.12, IC3.14, IC3.9, SJ3.3
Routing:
- net CLK28: track 262.3 -> 199.4 mm
- net CLK14: track 228.6 -> 191.4 mm
- net N$86: track 32.8 -> 0.00 mm, vias 2 -> 0
- net N$85: track 30.8 -> 0.00 mm
- net N$83: track 16.8 -> 0.00 mm
- net N$84: track 13.0 -> 0.00 mm
- net P1: track 215.2 -> 211.6 mm
